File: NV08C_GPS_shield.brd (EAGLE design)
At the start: 100 x 80 mm, 48 parts, among them IC1 MCP1702-3.3, IC2 74LVC1T45SOT23-HAND, IC3 74LVC1T45SOT23-HAND, IC4 74LVC1T45SOT23-HAND, IC5 74LVC1T45SOT23-HAND, IC6 74LVC1T45SOT23-HAND, IC7 74LVC1T45SOT23-HAND, X1 CONN-SMATHD-SMD-EDGE

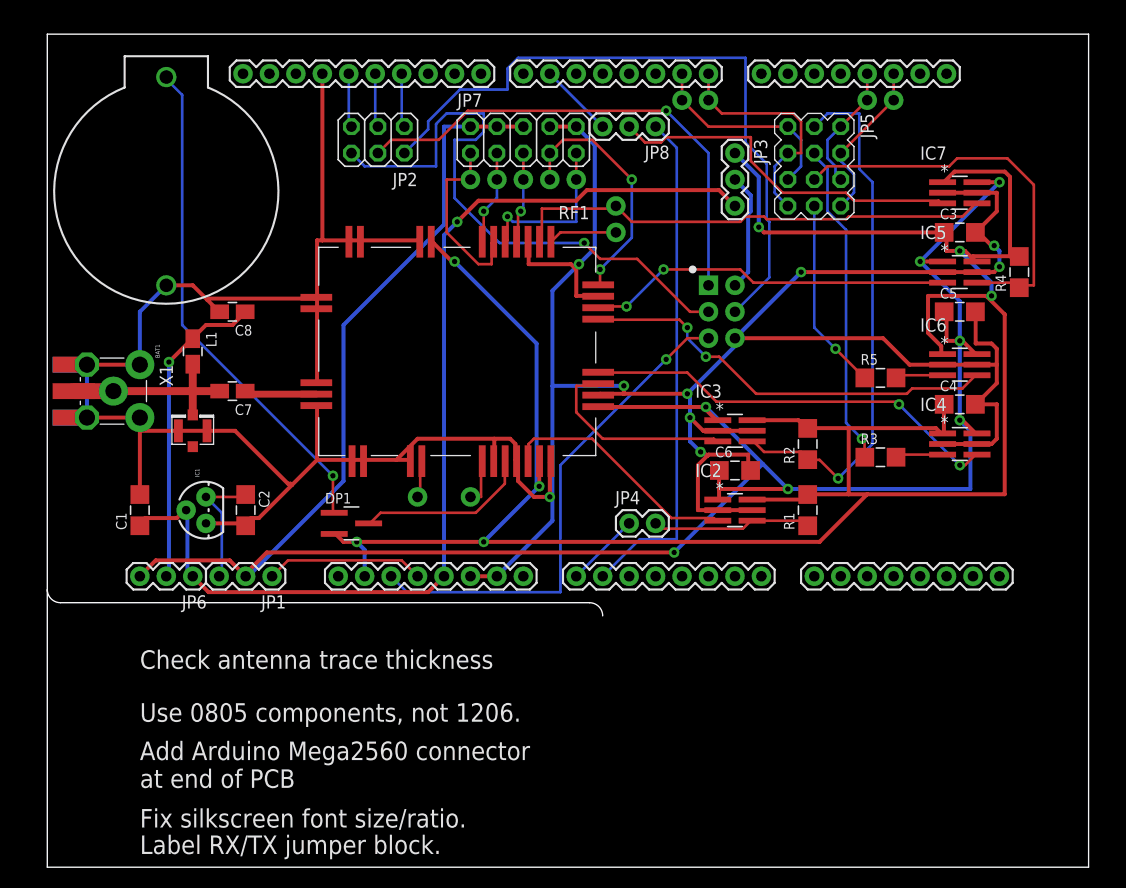
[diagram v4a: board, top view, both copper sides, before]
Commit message: Change PPS pin used. Add decoupling for NV08C module.
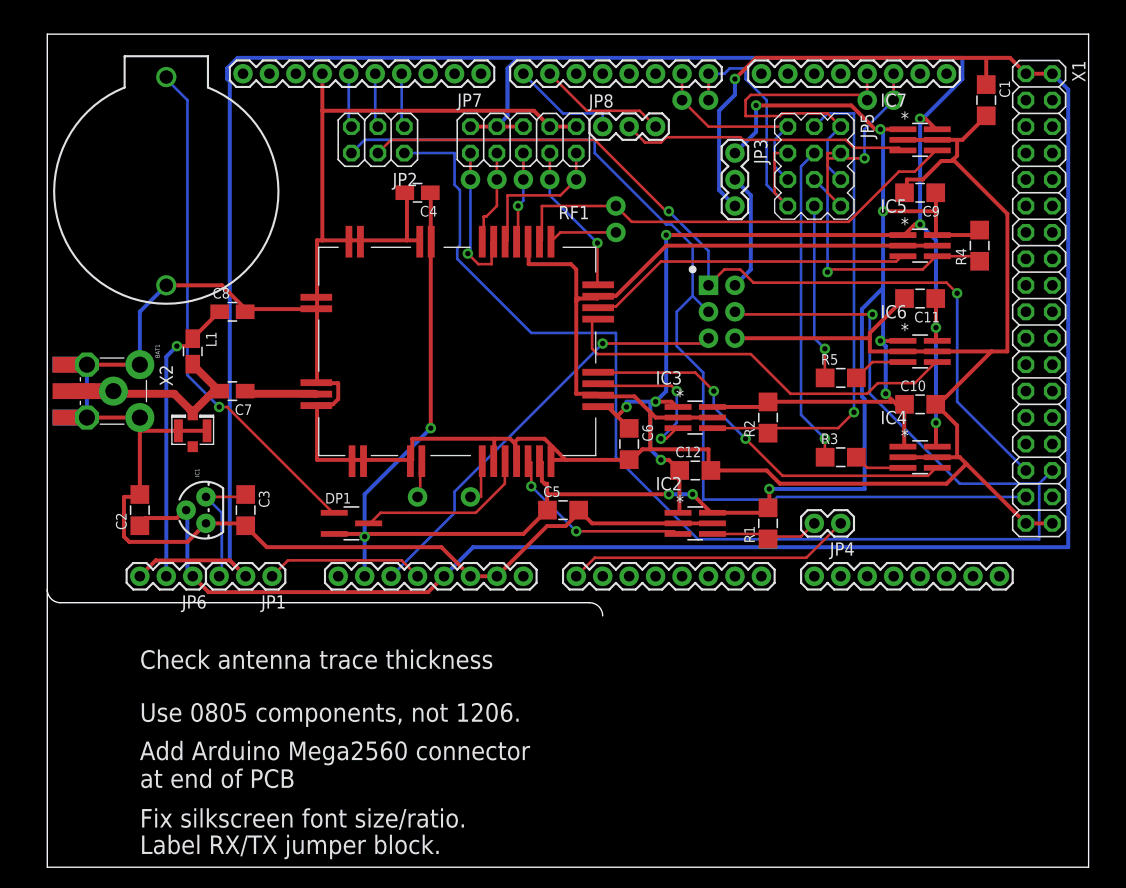
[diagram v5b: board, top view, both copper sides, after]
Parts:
- added C10, C11, C12, C9: 100n, SteveMarple:1206-HAND
- added X2: CONN-SMATHD-SMD-EDGE, SteveMarple:SMA-THD-EDGE
- C3, C5, C6: value 100n -> 1u
- C4: value 100n -> 22p; device SteveMarple:1206-HAND -> SteveMarple:0805-HAND
- X1: value CONN-SMATHD-SMD-EDGE -> MEGA2560; device SteveMarple:SMA-THD-EDGE -> pinhead:2X18
- moved C1 90.3 mm to (90.2, 73.7), turned to 270 degrees
- moved X1 89.3 mm to (95.2, 54.6)
- moved C3 73.6 mm to (19.1, 34.3), turned to 270 degrees
- moved C4 55.9 mm to (35.6, 64.8), turned to 180 degrees
- moved C5 42.6 mm to (49.5, 34.3)
- moved JP4 20.3 mm to (76.2, 33.0), turned to 180 degrees
- moved C6 10.5 mm to (55.9, 40.6), turned to 270 degrees
- moved C2 10.2 mm to (8.89, 34.3), turned to 90 degrees
- moved IC7 6.35 mm to (83.8, 69.8)
- moved JP8 5.08 mm to (53.3, 71.1), turned to 0 degrees
- moved IC5 4.58 mm to (83.8, 59.7)
- moved R2 4.58 mm to (69.2, 43.2)
- moved R4 4.58 mm to (89.5, 59.7)
- moved IC3 4.02 mm to (62.2, 43.2)
- moved IC2 4.02 mm to (62.2, 33.0)
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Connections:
- removed net A1: JP8.1, U$5.A1
- new net 7: JP8.1, U$5.7
- net +3V3: now also C11.1, C12.1; no longer C5.1
- net +5V: now also C2.1, X1.1, X1.2
- net GND: now also C10.2, C11.2, C12.2, C9.2, X1.35, X1.36, X2.GND@0, X2.GND@1, X2.GND@2, X2.GND@3, X2.GND@EDGE0, X2.GND@EDGE1, X2.GND@EDGE2, X2.GND@EDGE3; no longer X1.GND@0, X1.GND@1, X1.GND@2, X1.GND@3, X1.GND@EDGE0, X1.GND@EDGE1, X1.GND@EDGE2, X1.GND@EDGE3
- net IOREF: now also C10.1, C5.1, C9.1; no longer C3.1
- net MISO: now also X1.31
- net MOSI: now also X1.32
- net N$1: now also C3.1; no longer C2.1
- net N$4: now also X2.SIG, X2.SIG@EDGE; no longer X1.SIG, X1.SIG@EDGE
- net SCK: now also X1.33
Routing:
- net +5V: track 100.4 -> 192.5 mm
- net GND: track 373.2 -> 458.1 mm, vias 9 -> 0
- net MOSI: track 64.9 -> 137.3 mm, vias 0 -> 1
- net A1: track 49.1 -> 0.00 mm
- net SCK: track 57.1 -> 97.6 mm, vias 1 -> 0
- net MISO: track 47.8 -> 85.2 mm, vias 1 -> 2
- net +3V3: track 222.7 -> 255.2 mm, vias 7 -> 8
- net IOREF: track 237.0 -> 206.0 mm, vias 7 -> 10
- net A0: track 7.18 -> 27.5 mm
- net TX1: track 12.3 -> 31.9 mm
- net N$12: track 38.5 -> 24.9 mm, vias 0 -> 1
- net 7: track 0.00 -> 10.5 mm
- net GPIO6: track 24.0 -> 14.6 mm, vias 2 -> 1
- net PPS: track 34.9 -> 27.7 mm
- net N$2: track 48.4 -> 41.1 mm
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
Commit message: Minor layout and silkscreen fixes.
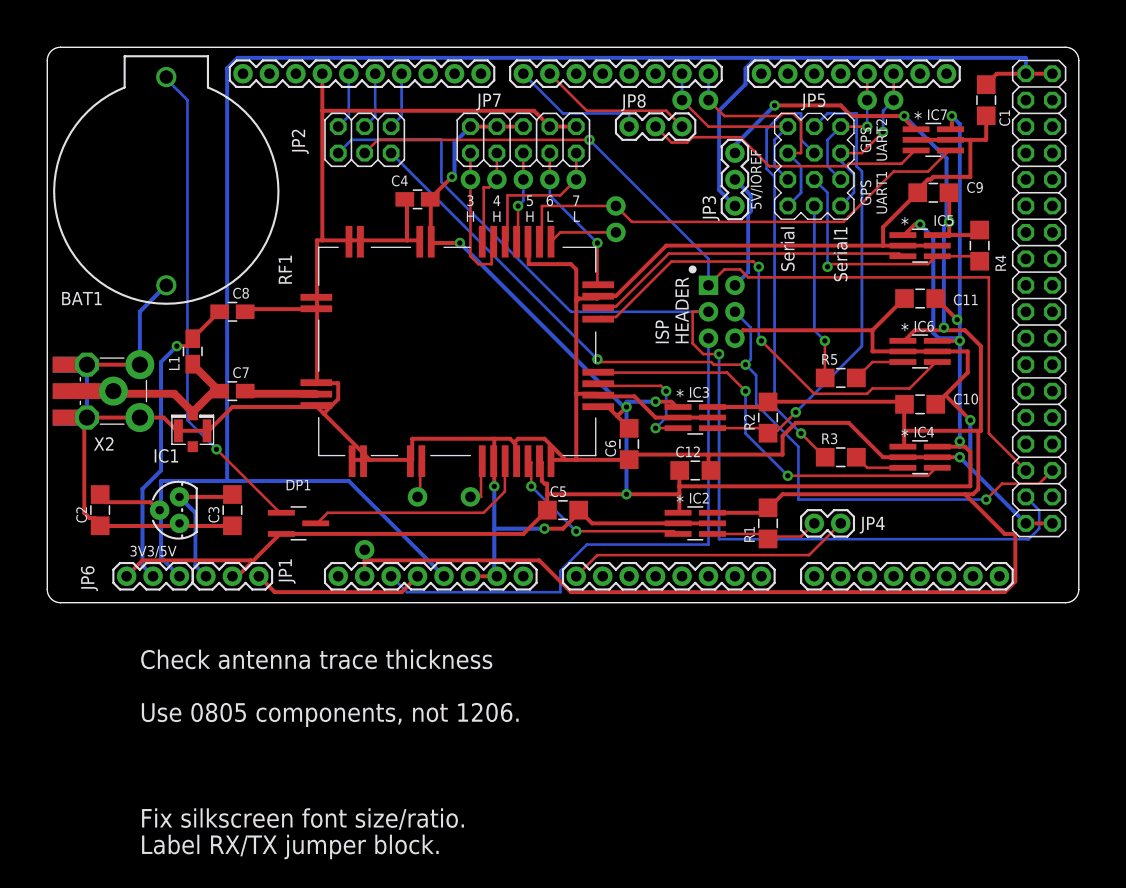
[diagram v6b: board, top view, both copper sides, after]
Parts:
- added X3: U.FL, SparkFun:U.FL
- DP1: value BAV70 -> BAS40-05
- JP1: value 3V3 SRC -> VREG/3V3
- JP2: value ALT ISP -> ISP LINK
- JP4: value (none) -> GPS !RESET! (A0)
- JP7: value (none) -> CONFIG
- JP8: value (none) -> PPS 7/6
- RF1: value (none) -> NV08C-CSM
- U$7: value U.FL -> PAD; device SparkFun:U.FL -> SteveMarple:PAD
- moved U$7 27.4 mm to (40.6, 35.6), turned to 270 degrees
- moved U$6 11.4 mm to (30.5, 30.5), turned to 0 degrees
- moved DP1 5.08 mm to (24.1, 33.0)
- moved C2 3.81 mm to (5.08, 34.3), turned to 270 degrees
- moved IC1 2.54 mm to (12.7, 34.3)
- moved JP8 2.54 mm to (55.9, 71.1)
- moved C9 1.27 mm to (85.1, 64.8)
- moved IC7 1.27 mm to (85.1, 69.8)
- moved JP6 1.27 mm to (12.7, 27.9)
- moved C3 1.27 mm to (17.8, 34.3)
- moved JP1 1.27 mm to (20.3, 27.9)
- moved JP2 1.27 mm to (30.5, 69.8)
- moved C4 0.63 mm to (35.6, 64.1)
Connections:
- net N$12 renamed GPS_RX1_IOREF
- net N$13 renamed GPS_TX2_IOREF
- net N$15 renamed GPS_TX1_IOREF
- net N$2 renamed !RESET
- net N$6 renamed GPS_RX2_IOREF
- net +3V3: now also C4.1, C5.1, DP1.2, RF1.P$26, RF1.P$8
- net GND: now also X3.P$1, X3.P$2; no longer U$7.P$1, U$7.P$2
- net IOREF: now also U$6.1; no longer C4.1, C5.1, DP1.2, RF1.P$26, RF1.P$8
- net N$20: now also U$7.1; no longer U$6.1
- net N$4: now also X3.P$3; no longer U$7.P$3
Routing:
- net MOSI: track 137.3 -> 89.0 mm, vias 1 -> 3
- net +3V3: track 255.2 -> 219.3 mm, vias 8 -> 10
- net GND: track 458.1 -> 426.2 mm, vias 0 -> 4
- net TX1: track 31.9 -> 13.8 mm, vias 0 -> 1
- net !RESET: track 41.1 -> 54.0 mm, vias 1 -> 0
- net GPS_TX2_IOREF: track 30.7 -> 42.1 mm
- net SCK: track 97.6 -> 105.3 mm, vias 0 -> 1
- net GPS_TX1: track 39.6 -> 45.4 mm, vias 0 -> 2
- net VBAT: track 16.8 -> 22.4 mm
- net RX0: track 28.1 -> 22.9 mm
- net +5V: track 192.5 -> 188.8 mm, vias 1 -> 0
- net MISO: track 85.2 -> 88.7 mm, vias 2 -> 1
- net GPS_RX2_IOREF: track 48.5 -> 45.2 mm
- net IOREF: track 206.0 -> 208.8 mm, vias 10 -> 4
- net RX1: track 19.7 -> 17.0 mm
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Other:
- board size 100 x 80 mm -> 99.1 x 53.3 mm
- board text added: "3 H"
- board text added: "3V3/5V"
- board text added: "4 H"
- board text added: "5 H"
- board text added: "5V/IOREF"
- board text added: "6 L"
- board text added: "7 L"
- board text added: "GPS UART1"
- board text added: "GPS UART2"
- board text added: "ISP HEADER"
- board text added: "Serial"
- board text added: "Serial1"
- board text removed: "Add Arduino Mega2560 connector at end of PCB"

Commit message: Layout and silkscreen changes. Ground pour added.
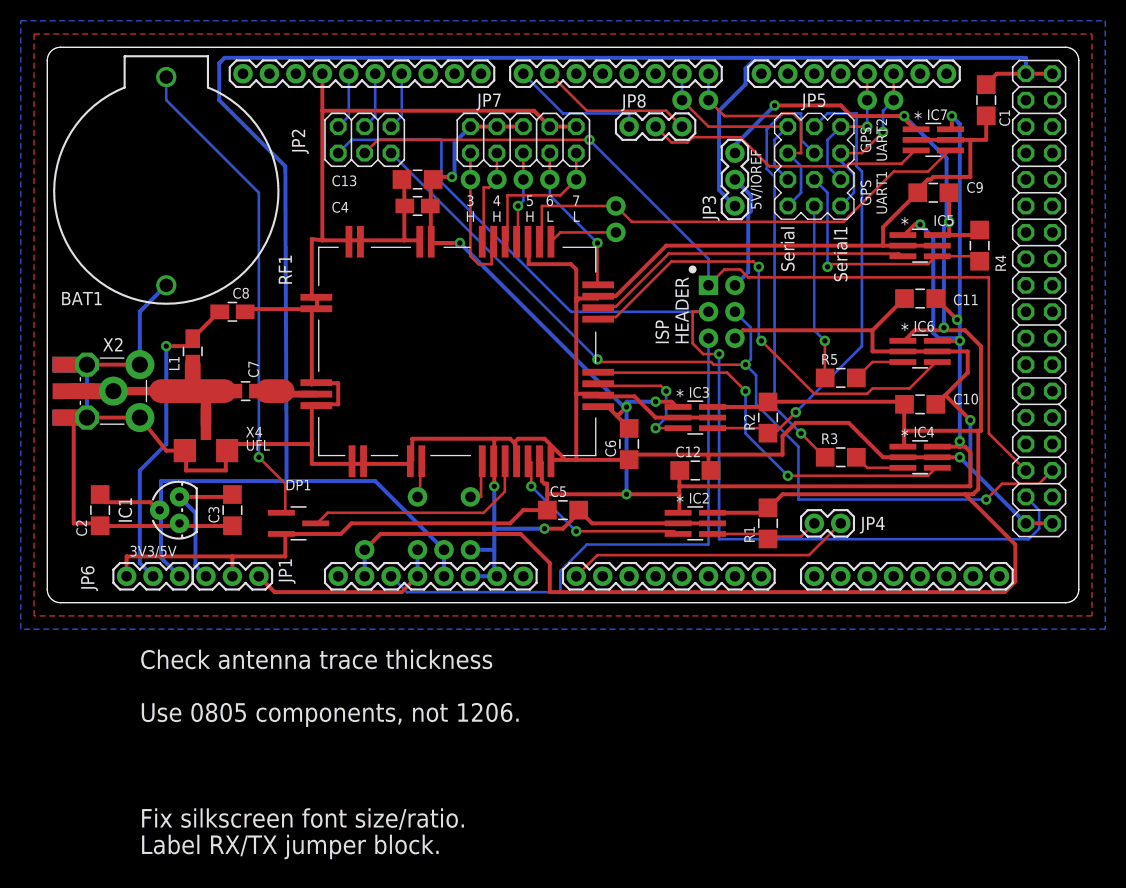
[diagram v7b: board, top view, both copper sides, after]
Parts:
- removed X3: U.FL, SparkFun:U.FL
- added C13: 1u, SteveMarple:1206-HAND
- added U$16, U$17, U$18: PAD, SteveMarple:PAD
- added X4: UFL, SteveMarple:CONN-UFL-HAND-SOLDERING
- moved C7 1.27 mm to (19.1, 45.7)
- moved C4 0.64 mm to (35.6, 63.5)
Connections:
- net +3V3: now also C13.1
- net +5V: now also U$17.1
- net 3V3_SHIELD: now also U$16.1
- net GND: now also C13.2, U$18.1, X4.GND@0, X4.GND@1; no longer X3.P$1, X3.P$2
- net N$4: now also X4.SIGNAL; no longer X3.P$3
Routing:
- net GND: track 426.2 -> 445.6 mm
- net N$4: track 16.0 -> 22.1 mm
- net +5V: track 188.8 -> 193.9 mm
- net +3V3: track 219.3 -> 222.5 mm
- net IOREF: track 208.8 -> 211.5 mm
- net 3V3_SHIELD: track 16.5 -> 19.0 mm
- net N$7: track 6.94 -> 5.69 mm
- net V_ANT: track 29.5 -> 30.3 mm
- added copper zone on layer 1, net GND
- added copper zone on layer 16, net GND

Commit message: Minor routing and silkscreen changes. Extra pads added.
Adding extra pads to access unused Arduino pins for easier hacking.
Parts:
- added U$19, U$20, U$21, U$22, U$23, U$24, U$25: PAD, SteveMarple:PAD
- moved R5 1.27 mm to (76.2, 48.3)
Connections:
- net N$20 renamed SLEEP_FLAG
- new net MEGA_28: U$24.1, X1.7
- new net MEGA_30: U$23.1, X1.9
- new net N$10: U$22.1, U$5.16
- new net N$2: U$19.1, U$5.19
- new net N$6: U$20.1, U$5.18
- new net N$9: U$21.1, U$5.17
- net GND: now also U$25.1
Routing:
- net PPS: track 27.6 -> 37.2 mm
- net IOREF: track 211.5 -> 215.7 mm
- net +3V3: track 222.5 -> 225.8 mm
- net GND: track 445.6 -> 448.9 mm
- net MEGA_30: track 0.00 -> 2.54 mm
- net MEGA_28: track 0.00 -> 2.54 mm
- net N$9: track 0.00 -> 2.54 mm
- net N$6: track 0.00 -> 2.54 mm
- net N$2: track 0.00 -> 2.54 mm
- net N$10: track 0.00 -> 2.54 mm
- net GPIO1: track 46.3 -> 48.2 mm
- net MOSI: track 89.0 -> 90.5 mm
- net N$1: track 14.0 -> 15.5 mm
- net SCK: track 105.3 -> 103.9 mm
- net GPS_TX1_IOREF: track 17.0 -> 15.7 mm
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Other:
- board text added: "Arduino NV08C GPS Shield"
- board text added: "GPIO0"
- board text added: "GPIO1"
- board text added: "GPIO2"
- board text added: "GPS 1"
- board text added: "GPS 2"
- board text added: "SERIAL"
- board text added: "SERIAL1"
- board text added: "SLEEP FLAG"
- board text added: "Steve Marple Lancaster University"
- board text removed: "Fix silkscreen font size/ratio."
- board text removed: "GPS UART1"
- board text removed: "GPS UART2"
- board text removed: "Label RX/TX jumper block."
- board text removed: "Serial"
- board text removed: "Serial1"
- board text removed: "Use 0805 components, not 1206."
